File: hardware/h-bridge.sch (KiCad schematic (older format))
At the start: 64 parts, among them P3 CONN_01X02, Q3 IRFP4468, Q4 IRFP4468, Q5 IRFP4468, Q6 IRFP4468, Q7 IRFP4468, Q8 IRFP4468, Q9 DMT10H010LK3, U12 Si8640, U13 MIC4127, U14 LM5102, U15 LM5102, U19 MIC4127, U20 Si8640

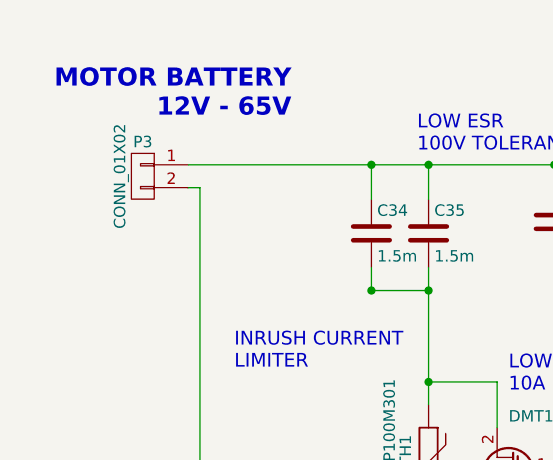
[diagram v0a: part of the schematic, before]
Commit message: Added most footprints, did non-power layout
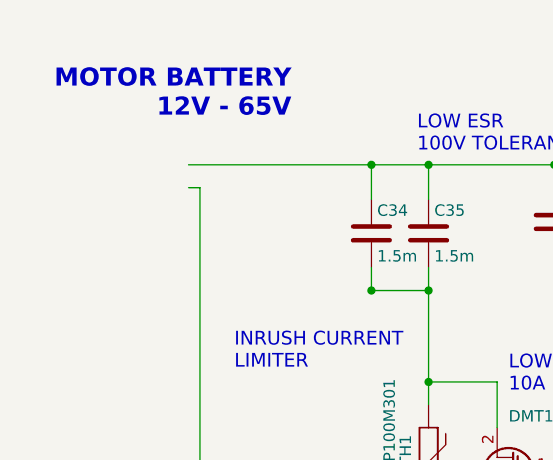
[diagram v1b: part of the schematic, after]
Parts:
- removed P3: CONN_01X02, symbol CONN_01X02
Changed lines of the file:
@@
 $EndComp
 $Comp
-L GNDPWR #PWR076
+L GNDPWR #PWR079
 U 1 1 5975827F
 P 7800 3600
-F 0 "#PWR076" H 7800 3400 50  0001 C CNN
+F 0 "#PWR079" H 7800 3400 50  0001 C CNN
 F 1 "GNDPWR" H 7800 3470 50  0000 C CNN
 F 2 "" H 7800 3550 50  0000 C CNN
@@
 Text Label 7650 1200 0    79   ~ 16
 VBUS
-$Comp
-L CONN_01X02 P3
-U 1 1 597582DA
-P 850 1250
-F 0 "P3" H 850 1400 50  0000 C CNN
-F 1 "CONN_01X02" V 950 1250 50  0000 C CNN
-F 2 "" H 850 1250 50  0001 C CNN
-F 3 "" H 850 1250 50  0000 C CNN
-	1    850  1250
-	-1   0    0    -1
-$EndComp
 $Comp
 L R R21
@@
 $EndComp
 $Comp
-L GNDPWR #PWR077
+L GNDPWR #PWR080
 U 1 1 59959CCF
 P 5200 1950
-F 0 "#PWR077" H 5200 1750 50  0001 C CNN
+F 0 "#PWR080" H 5200 1750 50  0001 C CNN
 F 1 "GNDPWR" H 5200 1820 50  0000 C CNN
 F 2 "" H 5200 1900 50  0000 C CNN
@@
 $EndComp
 $Comp
-L +12V_ISO #PWR078
+L +12V_ISO #PWR081
 U 1 1 5995F515
 P 5450 1550
-F 0 "#PWR078" H 5450 1400 50  0001 C CNN
+F 0 "#PWR081" H 5450 1400 50  0001 C CNN
 F 1 "+12V_ISO" H 5450 1690 50  0000 C CNN
 F 2 "" H 5450 1550 50  0000 C CNN
@@
 $EndComp
 $Comp
-L GNDPWR #PWR079
+L GNDPWR #PWR082
 U 1 1 5998917B
 P 10300 1950
-F 0 "#PWR079" H 10300 1750 50  0001 C CNN
+F 0 "#PWR082" H 10300 1750 50  0001 C CNN
 F 1 "GNDPWR" H 10300 1820 50  0000 C CNN
 F 2 "" H 10300 1900 50  0000 C CNN
@@
 $EndComp
 $Comp
-L +12V_ISO #PWR080
+L +12V_ISO #PWR083
 U 1 1 59989187
 P 10050 1550
-F 0 "#PWR080" H 10050 1400 50  0001 C CNN
+F 0 "#PWR083" H 10050 1400 50  0001 C CNN
 F 1 "+12V_ISO" H 10050 1690 50  0000 C CNN
 F 2 "" H 10050 1550 50  0000 C CNN
@@
 $EndComp
 $Comp
-L GNDPWR #PWR081
+L GNDPWR #PWR084
 U 1 1 599891AB
 P 9150 2950
-F 0 "#PWR081" H 9150 2750 50  0001 C CNN
+F 0 "#PWR084" H 9150 2750 50  0001 C CNN
 F 1 "GNDPWR" H 9150 2820 50  0000 C CNN
 F 2 "" H 9150 2900 50  0000 C CNN
@@
 $EndComp
 $Comp
-L GNDPWR #PWR082
+L GNDPWR #PWR085
 U 1 1 59967530
 P 6350 2950
-F 0 "#PWR082" H 6350 2750 50  0001 C CNN
+F 0 "#PWR085" H 6350 2750 50  0001 C CNN
 F 1 "GNDPWR" H 6350 2820 50  0000 C CNN
 F 2 "" H 6350 2900 50  0000 C CNN
@@
 LOW ESR\n100V TOLERANT
 $Comp
-L GNDPWR #PWR083
+L GNDPWR #PWR086
 U 1 1 599BCA83
 P 2100 3600
-F 0 "#PWR083" H 2100 3400 50  0001 C CNN
+F 0 "#PWR086" H 2100 3400 50  0001 C CNN
 F 1 "GNDPWR" H 2100 3470 50  0000 C CNN
 F 2 "" H 2100 3550 50  0000 C CNN
@@
 $EndComp
 $Comp
-L +3.3V #PWR084
+L +3.3V #PWR087
 U 1 1 599D3CAE
 P 8100 4400
-F 0 "#PWR084" H 8100 4250 50  0001 C CNN
+F 0 "#PWR087" H 8100 4250 50  0001 C CNN
 F 1 "+3.3V" H 8100 4540 50  0000 C CNN
 F 2 "" H 8100 4400 50  0000 C CNN
@@
 $EndComp
 $Comp
-L GND #PWR085
+L GND #PWR088
 U 1 1 599D3CC0
 P 7900 4750
-F 0 "#PWR085" H 7900 4500 50  0001 C CNN
+F 0 "#PWR088" H 7900 4500 50  0001 C CNN
 F 1 "GND" H 7900 4600 50  0000 C CNN
 F 2 "" H 7900 4750 50  0000 C CNN
@@
 $EndComp
 $Comp
-L +5V_ISO #PWR086
+L +5V_ISO #PWR089
 U 1 1 599D3CD5
 P 9200 4400
-F 0 "#PWR086" H 9200 4250 50  0001 C CNN
+F 0 "#PWR089" H 9200 4250 50  0001 C CNN
 F 1 "+5V_ISO" H 9200 4540 50  0000 C CNN
 F 2 "" H 9200 4400 50  0000 C CNN
@@
 $EndComp
 $Comp
-L GNDPWR #PWR087
+L GNDPWR #PWR090
 U 1 1 599D3CF4
 P 9400 4750
-F 0 "#PWR087" H 9400 4550 50  0001 C CNN
+F 0 "#PWR090" H 9400 4550 50  0001 C CNN
 F 1 "GNDPWR" H 9400 4620 50  0000 C CNN
 F 2 "" H 9400 4700 50  0000 C CNN
@@
 $EndComp
 $Comp
-L +12V_ISO #PWR088
+L +12V_ISO #PWR091
 U 1 1 59A0BCFD
 P 6150 3850
-F 0 "#PWR088" H 6150 3700 50  0001 C CNN
+F 0 "#PWR091" H 6150 3700 50  0001 C CNN
 F 1 "+12V_ISO" H 6150 3990 50  0000 C CNN
 F 2 "" H 6150 3850 50  0000 C CNN
@@
 $EndComp
 $Comp
-L GNDPWR #PWR089
+L GNDPWR #PWR092
 U 1 1 59A194F2
 P 5450 3600
-F 0 "#PWR089" H 5450 3400 50  0001 C CNN
+F 0 "#PWR092" H 5450 3400 50  0001 C CNN
 F 1 "GNDPWR" H 5450 3470 50  0000 C CNN
 F 2 "" H 5450 3550 50  0000 C CNN
@@
 $EndComp
 $Comp
-L GNDPWR #PWR090
+L GNDPWR #PWR093
 U 1 1 59A199E4
 P 10050 3600
-F 0 "#PWR090" H 10050 3400 50  0001 C CNN
+F 0 "#PWR093" H 10050 3400 50  0001 C CNN
 F 1 "GNDPWR" H 10050 3470 50  0000 C CNN
 F 2 "" H 10050 3550 50  0000 C CNN
@@
 $EndComp
 $Comp
-L GND #PWR091
+L GND #PWR094
 U 1 1 59A2238F
 P 8100 5950
-F 0 "#PWR091" H 8100 5700 50  0001 C CNN
+F 0 "#PWR094" H 8100 5700 50  0001 C CNN
 F 1 "GND" H 8100 5800 50  0000 C CNN
 F 2 "" H 8100 5950 50  0000 C CNN
@@
 $EndComp
 $Comp
-L GNDPWR #PWR092
+L GNDPWR #PWR095
 U 1 1 59A24543
 P 9200 6000
-F 0 "#PWR092" H 9200 5800 50  0001 C CNN
+F 0 "#PWR095" H 9200 5800 50  0001 C CNN
 F 1 "GNDPWR" H 9200 5870 50  0000 C CNN
 F 2 "" H 9200 5950 50  0000 C CNN
@@
 VBUS
 $Comp
-L GNDMBAT #PWR093
+L GNDMBAT #PWR096
 U 1 1 59C09326
 P 1000 3600
-F 0 "#PWR093" H 1000 3350 50  0001 C CNN
+F 0 "#PWR096" H 1000 3350 50  0001 C CNN
 F 1 "GNDMBAT" H 1000 3450 50  0000 C CNN
 F 2 "" H 1000 3600 50  0000 C CNN
@@
 $EndComp
 $Comp
-L +12V_ISO #PWR094
+L +12V_ISO #PWR097
 U 1 1 59CA0DB7
 P 6150 4700
-F 0 "#PWR094" H 6150 4550 50  0001 C CNN
+F 0 "#PWR097" H 6150 4550 50  0001 C CNN
 F 1 "+12V_ISO" H 6150 4840 50  0000 C CNN
 F 2 "" H 6150 4700 50  0000 C CNN
@@
 $EndComp
 $Comp
-L GNDPWR #PWR095
+L GNDPWR #PWR098
 U 1 1 59BAB965
 P 2900 7250
-F 0 "#PWR095" H 2900 7050 50  0001 C CNN
+F 0 "#PWR098" H 2900 7050 50  0001 C CNN
 F 1 "GNDPWR" H 2900 7120 50  0000 C CNN
 F 2 "" H 2900 7200 50  0000 C CNN
@@
 $EndComp
 $Comp
-L GND #PWR096
+L GND #PWR099
 U 1 1 59BAD34A
 P 1750 7250
-F 0 "#PWR096" H 1750 7000 50  0001 C CNN
+F 0 "#PWR099" H 1750 7000 50  0001 C CNN
 F 1 "GND" H 1750 7100 50  0000 C CNN
 F 2 "" H 1750 7250 50  0000 C CNN
@@
 $EndComp
 $Comp
-L +3.3V #PWR097
+L +3.3V #PWR0100
 U 1 1 59BAFE13
 P 1800 5700
-F 0 "#PWR097" H 1800 5550 50  0001 C CNN
+F 0 "#PWR0100" H 1800 5550 50  0001 C CNN
 F 1 "+3.3V" H 1800 5840 50  0000 C CNN
 F 2 "" H 1800 5700 50  0000 C CNN
@@
 $EndComp
 $Comp
-L GND #PWR098
+L GND #PWR0101
 U 1 1 59BAFE19
 P 1600 6050
-F 0 "#PWR098" H 1600 5800 50  0001 C CNN
+F 0 "#PWR0101" H 1600 5800 50  0001 C CNN
 F 1 "GND" H 1600 5900 50  0000 C CNN
 F 2 "" H 1600 6050 50  0000 C CNN
@@
 $EndComp
 $Comp
-L +5V_ISO #PWR099
+L +5V_ISO #PWR0102
 U 1 1 59BB121B
 P 2900 5700
-F 0 "#PWR099" H 2900 5550 50  0001 C CNN
+F 0 "#PWR0102" H 2900 5550 50  0001 C CNN
 F 1 "+5V_ISO" H 2900 5840 50  0000 C CNN
 F 2 "" H 2900 5700 50  0000 C CNN
@@
 $EndComp
 $Comp
-L GNDPWR #PWR0100
+L GNDPWR #PWR0103
 U 1 1 59BB1221
 P 3100 6050
-F 0 "#PWR0100" H 3100 5850 50  0001 C CNN
+F 0 "#PWR0103" H 3100 5850 50  0001 C CNN
 F 1 "GNDPWR" H 3100 5920 50  0000 C CNN
 F 2 "" H 3100 6000 50  0000 C CNN

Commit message: H-bridge decoupling, footprints, mechanical
- Finished H-bridge decoupling study and chose H-bridge caps
- Changed LT3471 inductors to those found in reference design,
  made footprints for them
- Swapped Si86xx isolator for Si80xx (smaller package)
- Updated heatsink footprint with correct screw sizes
- Created mechanical hole footprints (M3, M4 screws)
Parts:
- removed C36, C37, C55: 10u, Capacitors_SMD:C_1206, symbol C
- removed JP3, JP4: Jumper_NO_Small, Pin_Headers:Pin_Header_Straight_1x02, symbol Jumper_NO_Small
- removed U12, U20: Si8640, Housings_SOIC:SOIC-16_7.5x10.3mm_Pitch1.27mm, symbol Si8640
- added C56, C59, C61, C62, C64, C65, C66: 1u, Capacitors_SMD:C_1206, symbol C
- added U16, U20: Si8045AA, Housings_SSOP:QSOP-16_3.9x4.9mm_Pitch0.635mm, symbol Si8045AA
- C68: renamed from C56; value 10u -> 1u
- renumbered C60 to C50, C34 to C51, C35 to C52, C61 to C53, C40 to C54, C41 to C55, C42 to C57, C54 to C58, C43 to C60, C38 to C63, C44 to C67, C39 to C69, C45 to C70, C46 to C71, D6 to D13, D7 to D14, Q9 to Q4, Q4 to Q5, Q5 to Q6, Q6 to Q7, Q7 to Q8, Q8 to Q9, R26 to R37, R21 to R38, R22 to R39, R27 to R40, R53 to R41, R23 to R42, R49 to R43, R24 to R44, R25 to R45, R32 to R46, R33 to R47, R34 to R48, R35 to R49, R28 to R50, R29 to R51, R30 to R52, R36 to R53, R31 to R54, R37 to R55, U13 to U17, U19 to U18, U14 to U19, U15 to U21
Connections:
- wire segments 190 -> 193
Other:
- note added: "4A MAX RIPPLE\nCURRENT"
- note added: "MOTOR BATTERY\n12V - 65V\nSCREW CONNECT"
- note removed: "LOW ESR, ESL\n10A RIPPLE MAX"
- note removed: "LOW ESR\n100V TOLERANT"
- note removed: "MOTOR BATTERY\n12V - 65V"
- moved on the sheet: C51, C52, C68, Q4

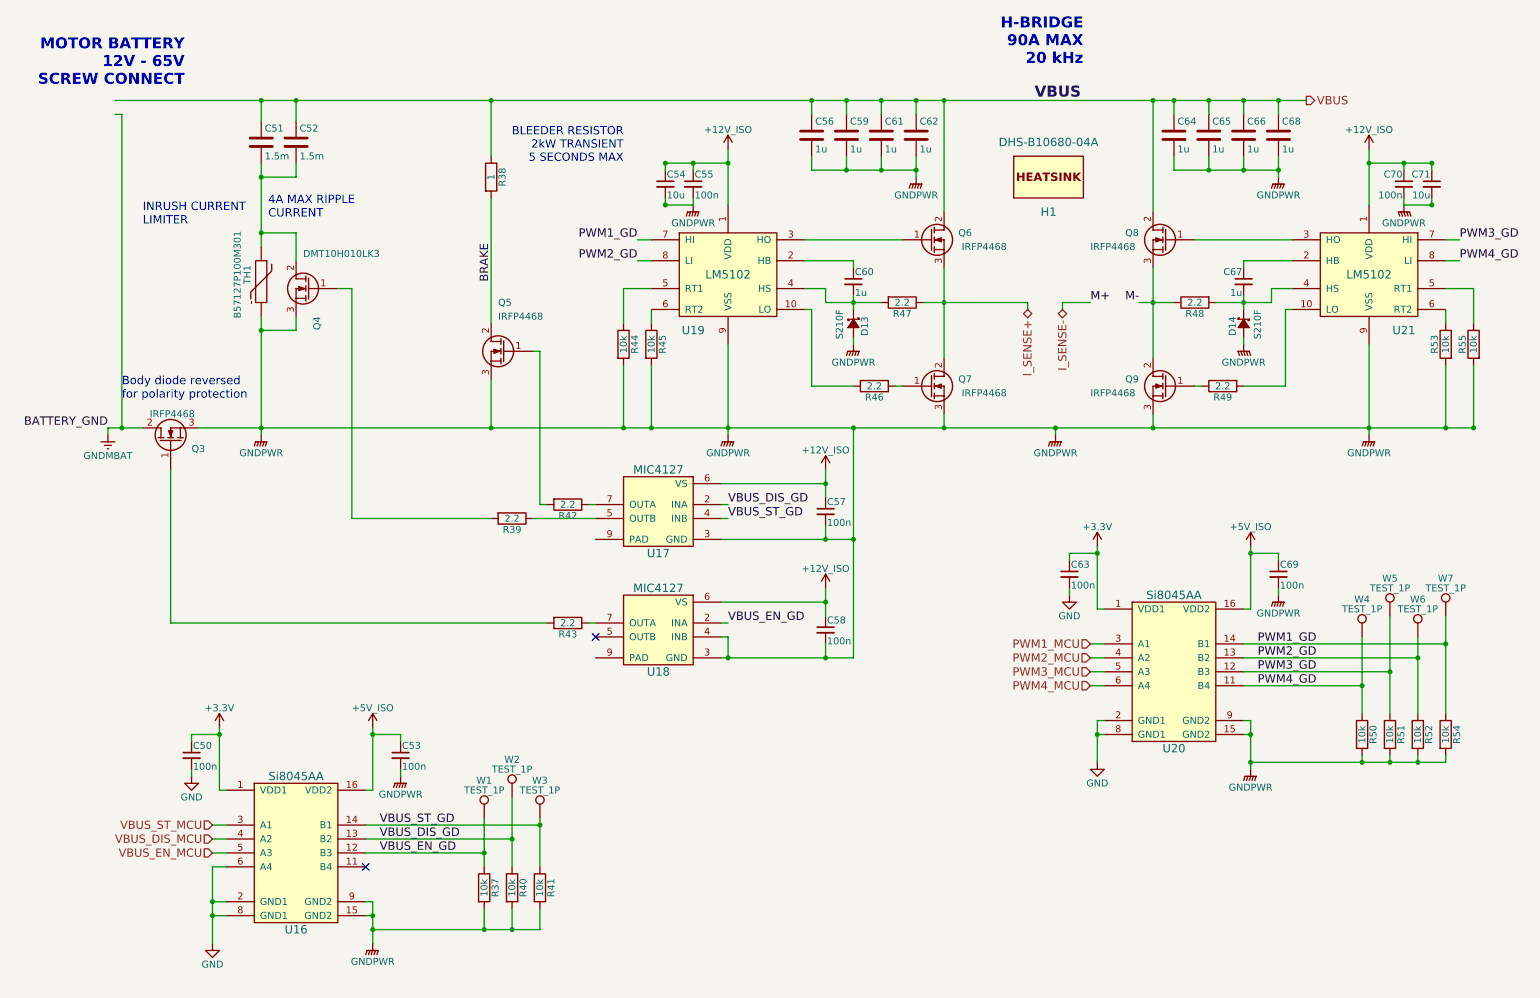
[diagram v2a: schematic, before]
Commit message: Bulk cap layout, diodes, lugs, leds, trimpots
- Moved H-bridge bulk capacitors to horizontal layout
- Changed H-bridge and fan diodes to 100V schottky
- Made 4AWG lug mount footprint, added lugs to BOM
- Tweaked LED resistor values, added LEDs to BOM
- Made trimpot footprint, added trimpots to BOM
- Added snubber to ferrite bead circuit; also added FB to BOM
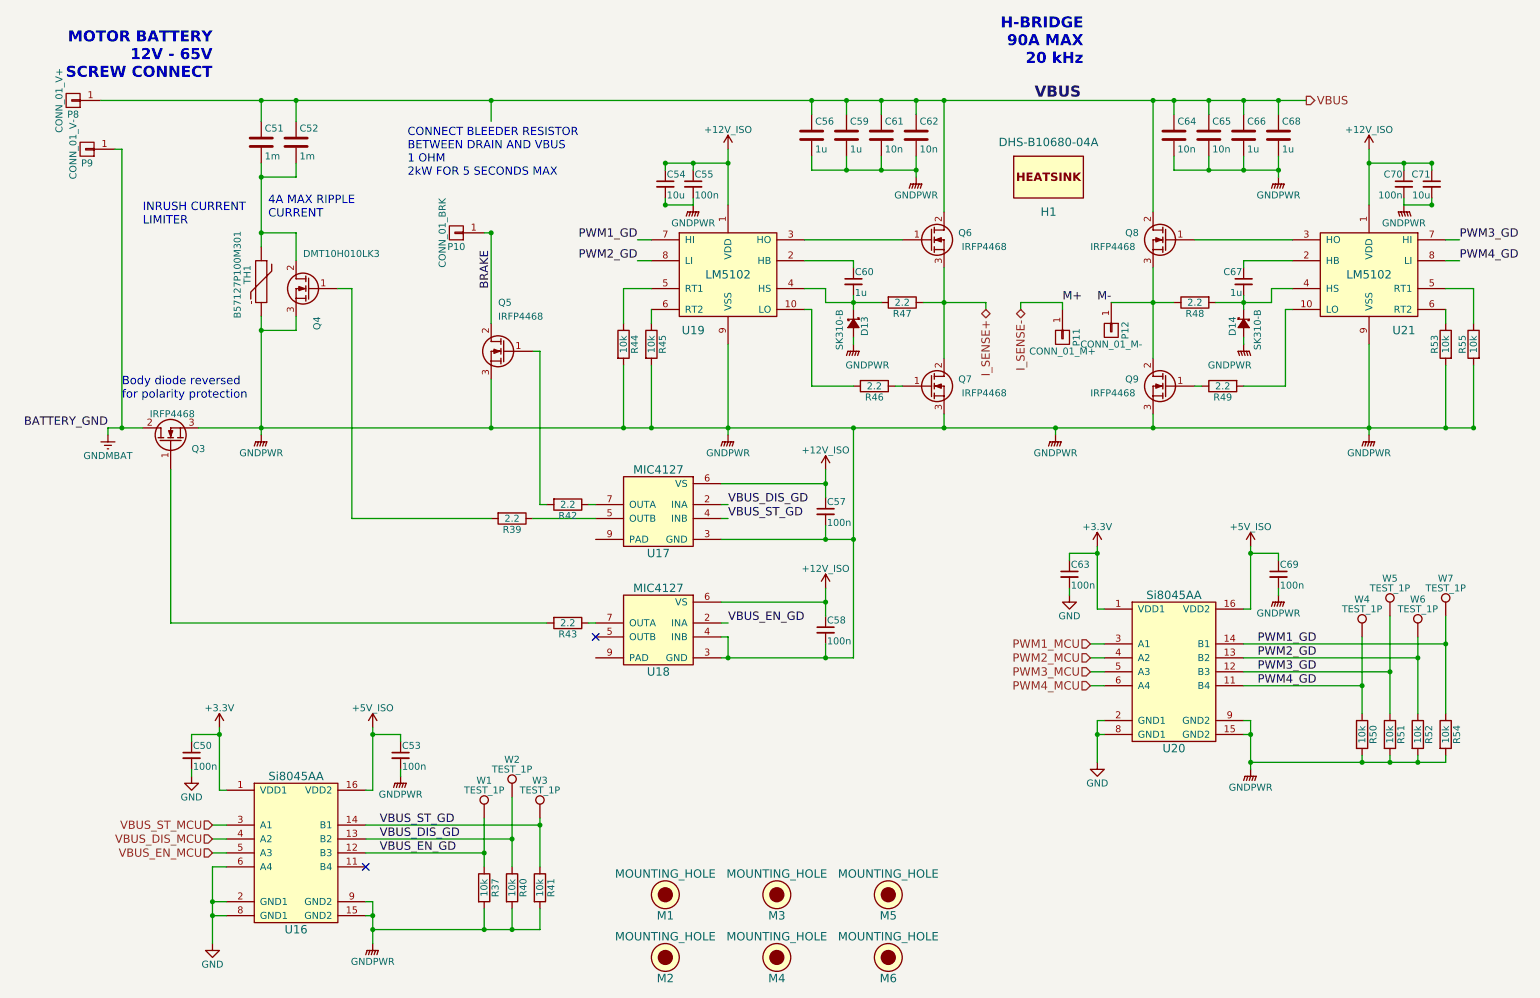
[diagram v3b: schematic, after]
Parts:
- removed R38: 1, Resistors_SMD:R_0603, symbol R
- added M1, M2, M3, M4, M5, M6: MOUNTING_HOLE, symbol MOUNTING_HOLE
- added P10: CONN_01_BRK, 2kwMotorController:M6_4AWG_LUG_TERM, symbol CONN_01X01
- added P11: CONN_01_M+, 2kwMotorController:M6_4AWG_LUG_TERM, symbol CONN_01X01
- added P12: CONN_01_M-, 2kwMotorController:M6_4AWG_LUG_TERM, symbol CONN_01X01
- added P8: CONN_01_V+, 2kwMotorController:M6_4AWG_LUG_TERM, symbol CONN_01X01
- added P9: CONN_01_V-, 2kwMotorController:M6_4AWG_LUG_TERM, symbol CONN_01X01
- C51, C52: value 1.5m -> 1m; footprint Capacitors_ThroughHole:C_Radial_D18_L36_P7.5 -> 2kwMotorController:Cap_Horizontal_D18_L36
- C61, C62, C64, C65: value 1u -> 10n
- D13, D14: value S210F -> SK310-B; footprint Diodes_SMD:SOD-123 -> 2kwMotorController:DO-214AA
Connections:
- net BRAKE: now also P10.1 (P1)
- net GNDMBAT: now also P9.1 (P1)
- net I_SENSE-: now also P11.1 (P1)
- net M-: now also P12.1 (P1)
- net VBUS: now also P8.1 (P1)
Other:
- note added: "CONNECT BLEEDER RESISTOR\nBETWEEN DRAIN AND VBUS\n1 OHM\n2kW FOR 5 SECONDS MAX"
- note removed: "BLEEDER RESISTOR\n2kW TRANSIENT\n5 SECONDS MAX"

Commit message: Inrush circuit, mounting hole position, temp sensor
- Split inrush circuit (one for each bulk cap). Replaced NTC
  thermistor with 2W power resistor. Replaced D2Pak MOSFET with
  LFPAK MOSFETs.
- Approximate position of mechanical holes chosen.
- Added thermistor temp sensor circuits.
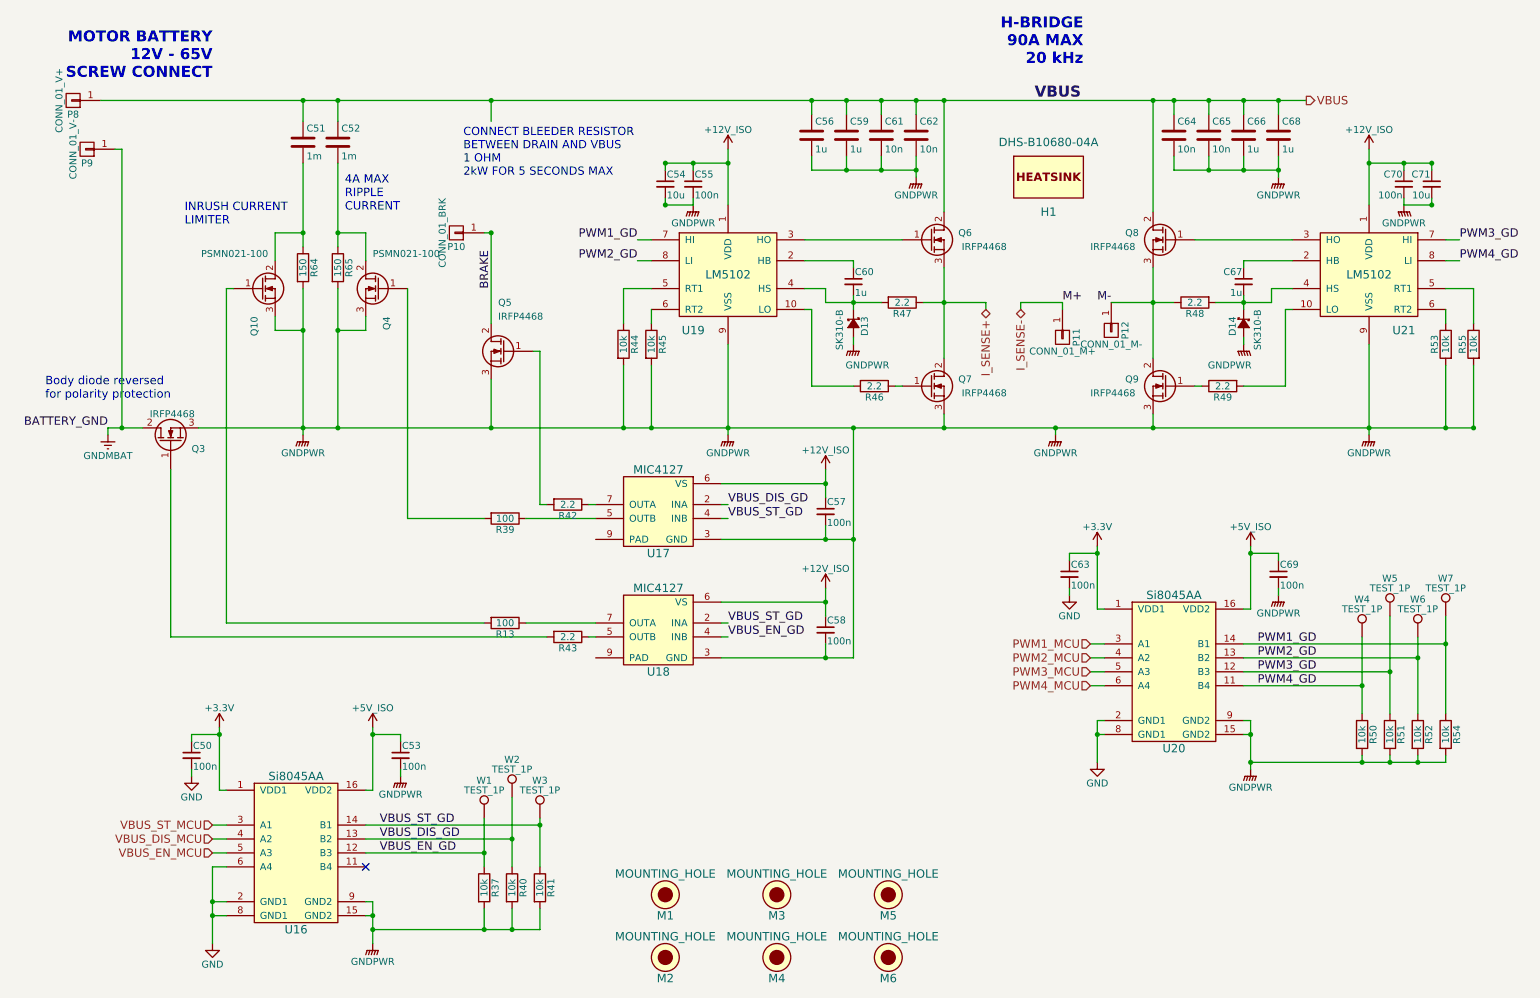
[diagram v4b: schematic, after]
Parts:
- removed TH1: B57127P100M301, Resistors_ThroughHole:Resistor_Vertical_RM7.5mm, symbol THERMISTOR
- added Q10: PSMN021-100, TO_SOT_Packages_SMD:SOT-669_LFPAK_ThermalVias-1, symbol Q_NMOS_GDS
- added R13: 100, Resistors_SMD:R_0603, symbol R
- added R64, R65: 150, 2kwMotorController:RESISTOR_FMP200, symbol R
- M1, M2, M3, M4, M5, M6: footprint (none) -> 2kwMotorController:M4-SCREW-HOLE
- Q4: value DMT10H010LK3 -> PSMN021-100; footprint TO_SOT_Packages_SMD:TO-252-2Lead -> TO_SOT_Packages_SMD:SOT-669_LFPAK_ThermalVias-1
- R39: value 2.2 -> 100
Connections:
- net GNDPWR: now also Q10.3 (S), R64.2, R65.2; no longer U18.4 (INB)
- net VBUS_EN_GD: now also U18.4 (INB); no longer U18.2 (INA)
- net VBUS_ST_GD: now also U18.2 (INA)
- net at C52.2, Q4.2 (D): now also R65.1; no longer C51.2
- net at U18.5 (OUTB): now also R43.1
- net at U18.7 (OUTA): now also R13.1; no longer R43.1
- new net: C51.2, Q10.2 (D), R64.1
- new net: Q10.1 (G), R13.2
- no-connect marks 2 -> 1
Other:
- note added: "4A MAX \nRIPPLE\nCURRENT"
- note removed: "4A MAX RIPPLE\nCURRENT"
- moved on the sheet: C51, C52, Q4, R39, R43
